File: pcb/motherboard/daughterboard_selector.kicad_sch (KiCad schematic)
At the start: 9 parts, among them IC1 74HC138BQ,115, IC2 74HC138BQ,115, IC3 74HC138BQ,115, IC4 74HC138BQ,115

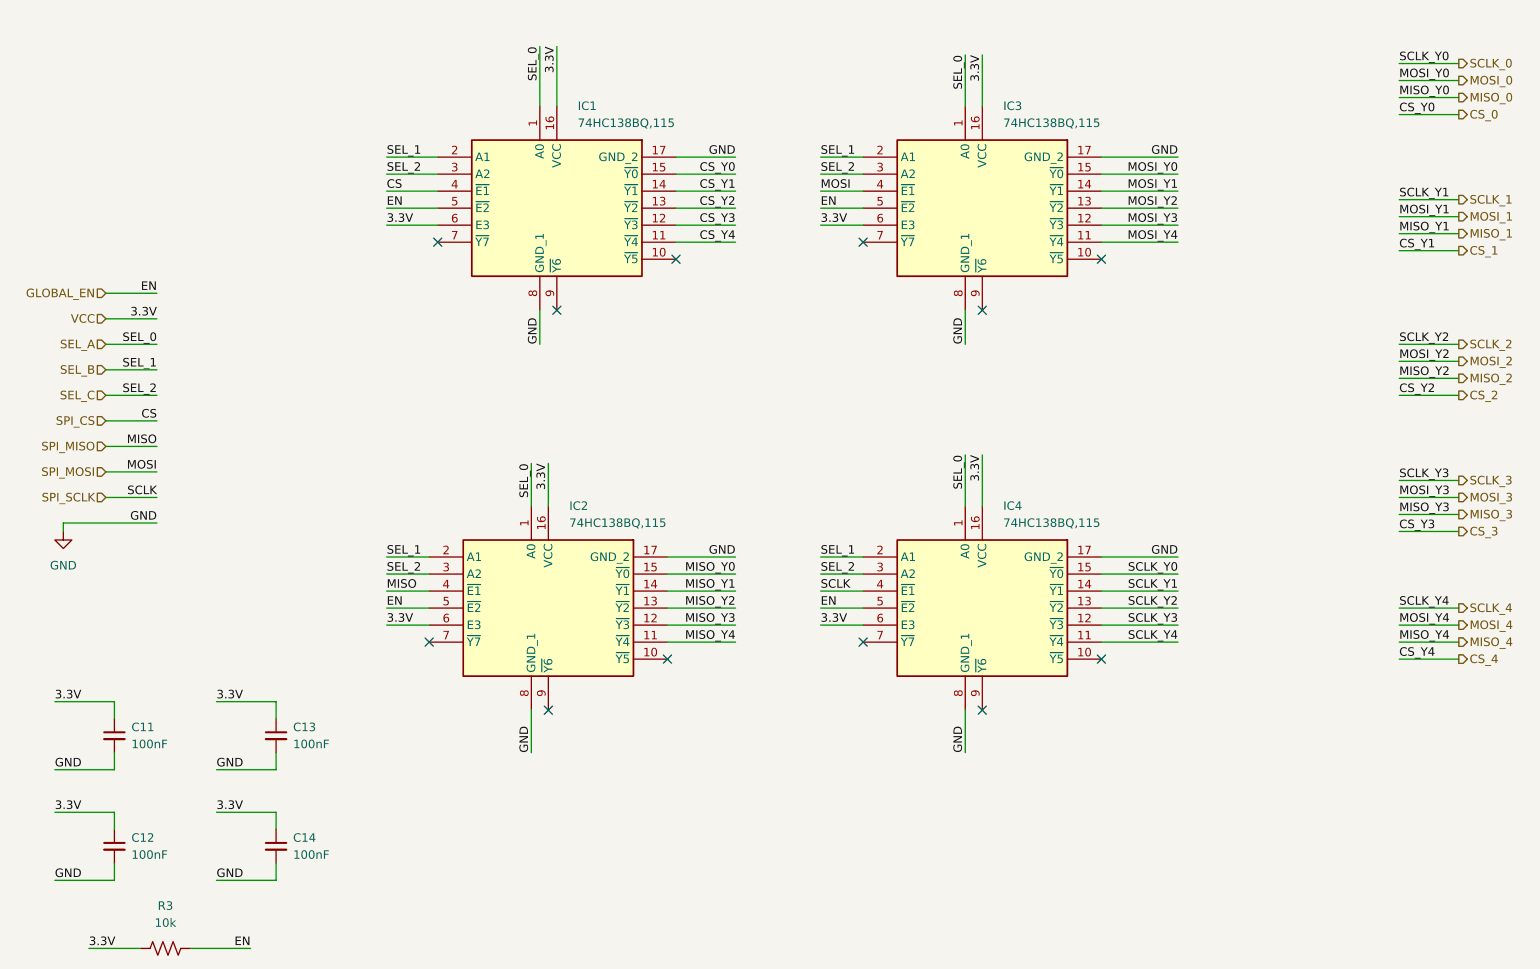
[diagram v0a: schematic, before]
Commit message: Fix DaughterBoard Selector use 74HC138 exclusively for Chip Select.
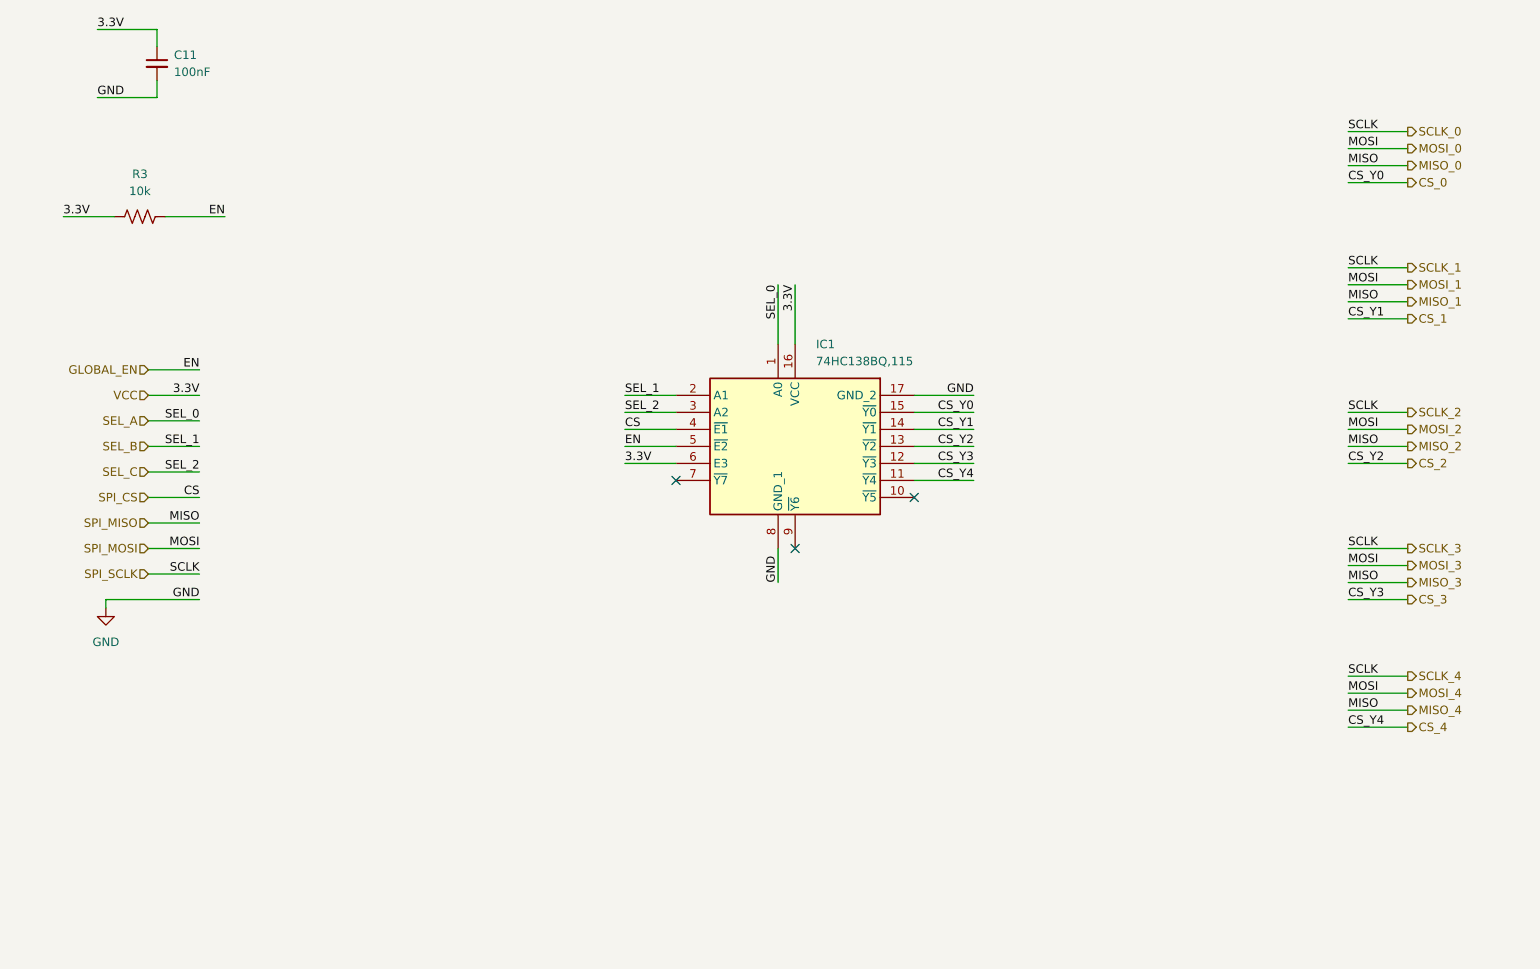
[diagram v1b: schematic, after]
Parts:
- removed C12, C13, C14: 100nF, symbol Device:C_Small
- removed IC2, IC3, IC4: 74HC138BQ,115, 74HC138BQ115, symbol 74HC138BQ_115:74HC138BQ,115
- C11: footprint (none) -> Capacitor_SMD:C_0603_1608Metric
- R3: footprint (none) -> Resistor_SMD:R_0603_1608Metric
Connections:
- no-connect marks 12 -> 3
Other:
- moved on the sheet: C11, IC1, R3
